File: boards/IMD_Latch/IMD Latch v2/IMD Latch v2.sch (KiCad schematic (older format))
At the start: 17 parts, among them J1 micromatch_female_RA_8, J2 Ultrafit_2, K1 G5Q-1A4-DC5-5V, Q1 SSM3K333R, U1 CD4043BPWR

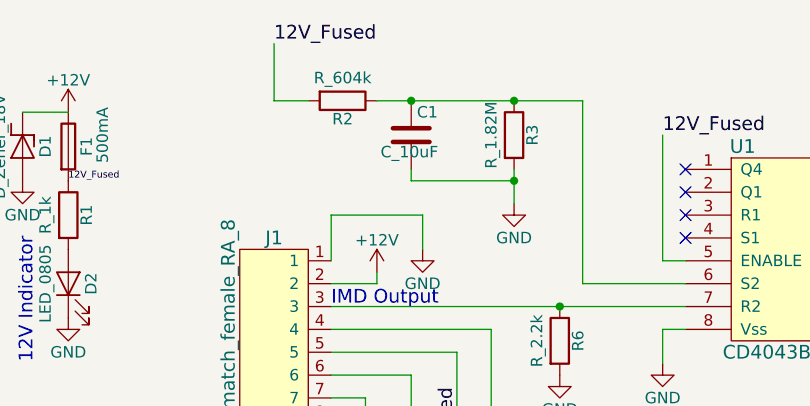
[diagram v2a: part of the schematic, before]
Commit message: IMD Latch v2 finished Layout/Routing
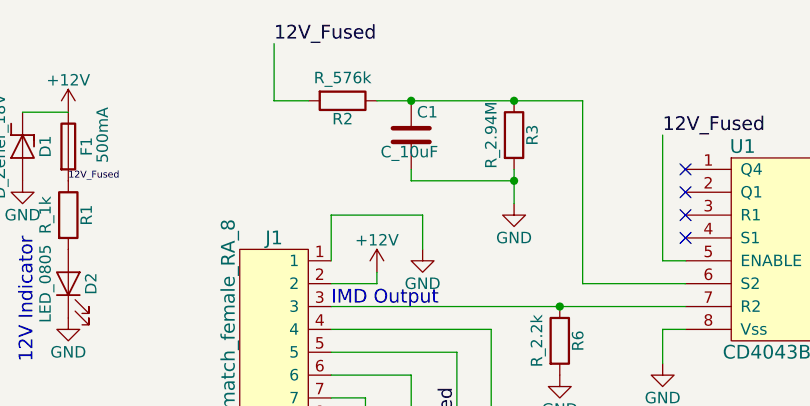
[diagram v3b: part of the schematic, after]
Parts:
- removed R2: R_604k, footprints:R_0805_OEM, symbol R_604k
- removed R3: R_1.82M, footprints:R_0805_OEM, symbol R_1.82M
- added R2: R_576k, footprints:R_0805_OEM, symbol R_576k
- added R3: R_2.94M, footprints:R_0805_OEM, symbol R_2.94M
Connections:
- net 12V_Fused: now also R2.2
- net GND: now also R3.2
- net at C1.1, U1.6 (S2): now also R2.1, R3.1
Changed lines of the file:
@@
 $EndComp
 $Comp
-L +12V #PWR3
+L +12V #PWR01
 U 1 1 59E04C1A
 P 2800 2850
-F 0 "#PWR3" H 2800 2700 50  0001 C CNN
+F 0 "#PWR01" H 2800 2700 50  0001 C CNN
 F 1 "+12V" H 2800 2990 50  0000 C CNN
 F 2 "" H 2800 2850 50  0001 C CNN
@@
 $EndComp
 $Comp
-L GND #PWR4
+L GND #PWR02
 U 1 1 59E0588D
 P 2800 3750
-F 0 "#PWR4" H 2800 3500 50  0001 C CNN
+F 0 "#PWR02" H 2800 3500 50  0001 C CNN
 F 1 "GND" H 2800 3600 50  0000 C CNN
 F 2 "" H 2800 3750 50  0001 C CNN
@@
 $EndComp
 $Comp
-L PWR_FLAG #FLG1
+L PWR_FLAG #FLG03
 U 1 1 59E0A741
 P 2600 4650
-F 0 "#FLG1" H 2600 4725 50  0001 C CNN
+F 0 "#FLG03" H 2600 4725 50  0001 C CNN
 F 1 "PWR_FLAG" H 2600 4800 50  0000 C CNN
 F 2 "" H 2600 4650 50  0001 C CNN
@@
 $EndComp
 $Comp
-L PWR_FLAG #FLG2
+L PWR_FLAG #FLG04
 U 1 1 59E0A7A5
 P 3100 4650
-F 0 "#FLG2" H 3100 4725 50  0001 C CNN
+F 0 "#FLG04" H 3100 4725 50  0001 C CNN
 F 1 "PWR_FLAG" H 3100 4800 50  0000 C CNN
 F 2 "" H 3100 4650 50  0001 C CNN
@@
 $EndComp
 $Comp
-L +12V #PWR2
+L +12V #PWR05
 U 1 1 59E0A7D7
 P 2600 4650
-F 0 "#PWR2" H 2600 4500 50  0001 C CNN
+F 0 "#PWR05" H 2600 4500 50  0001 C CNN
 F 1 "+12V" H 2600 4790 50  0000 C CNN
 F 2 "" H 2600 4650 50  0001 C CNN
@@
 $EndComp
 $Comp
-L GND #PWR5
+L GND #PWR06
 U 1 1 59E0A859
 P 3100 4650
-F 0 "#PWR5" H 3100 4400 50  0001 C CNN
+F 0 "#PWR06" H 3100 4400 50  0001 C CNN
 F 1 "GND" H 3100 4500 50  0000 C CNN
 F 2 "" H 3100 4650 50  0001 C CNN
@@
 $EndComp
 $Comp
-L GND #PWR1
+L GND #PWR07
 U 1 1 59F277D6
 P 2600 3150
-F 0 "#PWR1" H 2600 2900 50  0001 C CNN
+F 0 "#PWR07" H 2600 2900 50  0001 C CNN
 F 1 "GND" H 2600 3000 50  0000 C CNN
 F 2 "" H 2600 3150 50  0001 C CNN
@@
 $EndComp
 $Comp
-L +12V #PWR7
+L +12V #PWR08
 U 1 1 5A028E2B
 P 4150 3550
-F 0 "#PWR7" H 4150 3400 50  0001 C CNN
+F 0 "#PWR08" H 4150 3400 50  0001 C CNN
 F 1 "+12V" H 4150 3690 50  0000 C CNN
 F 2 "" H 4150 3550 50  0001 C CNN
@@
 $EndComp
 $Comp
-L GND #PWR6
+L GND #PWR09
 U 1 1 5A028E67
 P 4100 4450
-F 0 "#PWR6" H 4100 4200 50  0001 C CNN
+F 0 "#PWR09" H 4100 4200 50  0001 C CNN
 F 1 "GND" H 4100 4300 50  0000 C CNN
 F 2 "" H 4100 4450 50  0001 C CNN
@@
 $EndComp
 $Comp
-L GND #PWR8
+L GND #PWR010
 U 1 1 5A028F0E
 P 4300 4450
-F 0 "#PWR8" H 4300 4200 50  0001 C CNN
+F 0 "#PWR010" H 4300 4200 50  0001 C CNN
 F 1 "GND" H 4300 4300 50  0000 C CNN
 F 2 "" H 4300 4450 50  0001 C CNN
@@
 $EndComp
 $Comp
-L GND #PWR10
+L GND #PWR011
 U 1 1 5A028F4A
 P 4650 4450
-F 0 "#PWR10" H 4650 4200 50  0001 C CNN
+F 0 "#PWR011" H 4650 4200 50  0001 C CNN
 F 1 "GND" H 4650 4300 50  0000 C CNN
 F 2 "" H 4650 4450 50  0001 C CNN
@@
 12V_Fused
 $Comp
-L GND #PWR9
+L GND #PWR012
 U 1 1 5A02994C
 P 4350 3450
-F 0 "#PWR9" H 4350 3200 50  0001 C CNN
+F 0 "#PWR012" H 4350 3200 50  0001 C CNN
 F 1 "GND" H 4350 3300 50  0000 C CNN
 F 2 "" H 4350 3450 50  0001 C CNN
@@
 $EndComp
 $Comp
-L GND #PWR16
+L GND #PWR013
 U 1 1 5A02B918
 P 7500 4100
-F 0 "#PWR16" H 7500 3850 50  0001 C CNN
+F 0 "#PWR013" H 7500 3850 50  0001 C CNN
 F 1 "GND" H 7500 3950 50  0000 C CNN
 F 2 "" H 7500 4100 50  0001 C CNN
@@
 $EndComp
 $Comp
-L GND #PWR13
+L GND #PWR014
 U 1 1 5A055F8E
 P 5400 3950
-F 0 "#PWR13" H 5400 3700 50  0001 C CNN
+F 0 "#PWR014" H 5400 3700 50  0001 C CNN
 F 1 "GND" H 5400 3800 50  0000 C CNN
 F 2 "" H 5400 3950 50  0001 C CNN
@@
 $EndComp
 $Comp
-L GND #PWR15
+L GND #PWR015
 U 1 1 5A057A89
 P 7050 4550
-F 0 "#PWR15" H 7050 4300 50  0001 C CNN
+F 0 "#PWR015" H 7050 4300 50  0001 C CNN
 F 1 "GND" H 7050 4400 50  0000 C CNN
 F 2 "" H 7050 4550 50  0001 C CNN
@@
 $EndComp
 $Comp
-L GND #PWR11
+L GND #PWR016
 U 1 1 5A05A2C9
 P 4750 3250
-F 0 "#PWR11" H 4750 3000 50  0001 C CNN
+F 0 "#PWR016" H 4750 3000 50  0001 C CNN
 F 1 "GND" H 4750 3100 50  0000 C CNN
 F 2 "" H 4750 3250 50  0001 C CNN
@@
 $EndComp
 $Comp
-L GND #PWR14
+L GND #PWR017
 U 1 1 5A054F56
 P 6700 4550
-F 0 "#PWR14" H 6700 4300 50  0001 C CNN
+F 0 "#PWR017" H 6700 4300 50  0001 C CNN
 F 1 "GND" H 6700 4400 50  0000 C CNN
 F 2 "" H 6700 4550 50  0001 C CNN
@@
 $EndComp
 $Comp
-L GND #PWR12
+L GND #PWR018
 U 1 1 5A077481
 P 4950 4000
-F 0 "#PWR12" H 4950 3750 50  0001 C CNN
+F 0 "#PWR018" H 4950 3750 50  0001 C CNN
 F 1 "GND" H 4950 3850 50  0000 C CNN
 F 2 "" H 4950 4000 50  0001 C CNN
@@
 Text Notes 3950 3700 0    60   ~ 0
 IMD Output
-$Comp
-L R_604k R2
-U 1 1 5A07892D
-P 4000 2800
-F 0 "R2" V 4080 2800 50  0000 C CNN
-F 1 "R_604k" V 3900 2800 50  0000 C CNN
-F 2 "footprints:R_0805_OEM" H 3930 2800 50  0001 C CNN
-F 3 "https://www.seielect.com/Catalog/SEI-RMCF_RMCP.pdf" H 4080 2800 50  0001 C CNN
-F 4 "Digi-Key" H 4000 2800 60  0001 C CNN "MFN"
-F 5 "RMCF0805FT604KCT-ND" H 4000 2800 60  0001 C CNN "MPN"
-F 6 "Value" H 4000 2800 60  0001 C CNN "Package"
-F 7 "https://www.digikey.com/product-detail/en/stackpole-electronics-inc/RMCF0805FT604K/RMCF0805FT604KCT-ND/4425214" H 4480 3200 60  0001 C CNN "PurchasingLink"
-	1    4000 2800
-	0    1    1    0
-$EndComp
-$Comp
-L R_1.82M R3
-U 1 1 5A07897A
-P 4750 2950
-F 0 "R3" V 4830 2950 50  0000 C CNN
-F 1 "R_1.82M" V 4650 2950 50  0000 C CNN
-F 2 "footprints:R_0805_OEM" H 4680 2950 50  0001 C CNN
-F 3 "https://www.seielect.com/Catalog/SEI-RMCF_RMCP.pdf" H 4830 2950 50  0001 C CNN
-F 4 "Digi-Key" H 4750 2950 60  0001 C CNN "MFN"
-F 5 "RMCF0805FT1M82CT-ND" H 4750 2950 60  0001 C CNN "MPN"
-F 6 "Value" H 4750 2950 60  0001 C CNN "Package"
-F 7 "https://www.digikey.com/product-detail/en/stackpole-electronics-inc/RMCF0805FT1M82/RMCF0805FT1M82CT-ND/2418309" H 5230 3350 60  0001 C CNN "PurchasingLink"
-	1    4750 2950
-	1    0    0    -1
-$EndComp
 Connection ~ 4950 3700
 $Comp
@@
 Wire Wire Line
 	7150 3500 7150 3350
+$Comp
+L R_2.94M R3
+U 1 1 5A08F396
+P 4750 2950
+F 0 "R3" V 4830 2950 50  0000 C CNN
+F 1 "R_2.94M" V 4650 2950 50  0000 C CNN
+F 2 "footprints:R_0805_OEM" H 4680 2950 50  0001 C CNN
+F 3 "http://www.vishay.com/docs/20035/dcrcwe3.pdf" H 4830 2950 50  0001 C CNN
+F 4 "Digi-Key" H 4750 2950 60  0001 C CNN "MFN"
+F 5 "541-2.94MCCT-ND" H 4750 2950 60  0001 C CNN "MPN"
+F 6 "Value" H 4750 2950 60  0001 C CNN "Package"
+F 7 "https://www.digikey.com/product-detail/en/vishay-dale/CRCW08052M94FKEA/541-2.94MCCT-ND/1181178" H 5230 3350 60  0001 C CNN "PurchasingLink"
+	1    4750 2950
+	1    0    0    -1
+$EndComp
+$Comp
+L R_576k R2
+U 1 1 5A08F41B
+P 4000 2800
+F 0 "R2" V 4080 2800 50  0000 C CNN
+F 1 "R_576k" V 3900 2800 50  0000 C CNN
+F 2 "footprints:R_0805_OEM" H 3930 2800 50  0001 C CNN
+F 3 "http://www.vishay.com/docs/20035/dcrcwe3.pdf" H 4080 2800 50  0001 C CNN
+F 4 "Digi-Key" H 4000 2800 60  0001 C CNN "MFN"
+F 5 "541-576KCCT-ND" H 4000 2800 60  0001 C CNN "MPN"
+F 6 "Value" H 4000 2800 60  0001 C CNN "Package"
+F 7 "https://www.digikey.com/product-detail/en/vishay-dale/CRCW0805576KFKEA/541-576KCCT-ND/1181100" H 4480 3200 60  0001 C CNN "PurchasingLink"
+	1    4000 2800
+	0    1    1    0
+$EndComp
 $EndSCHEMATC
